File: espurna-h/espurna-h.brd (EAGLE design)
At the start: 50 x 50 mm, 51 parts, among them IC1 AMS1117-3.3, IC2 ESP-12-SMD, IC3 PC817CS, IC4 HLW8012

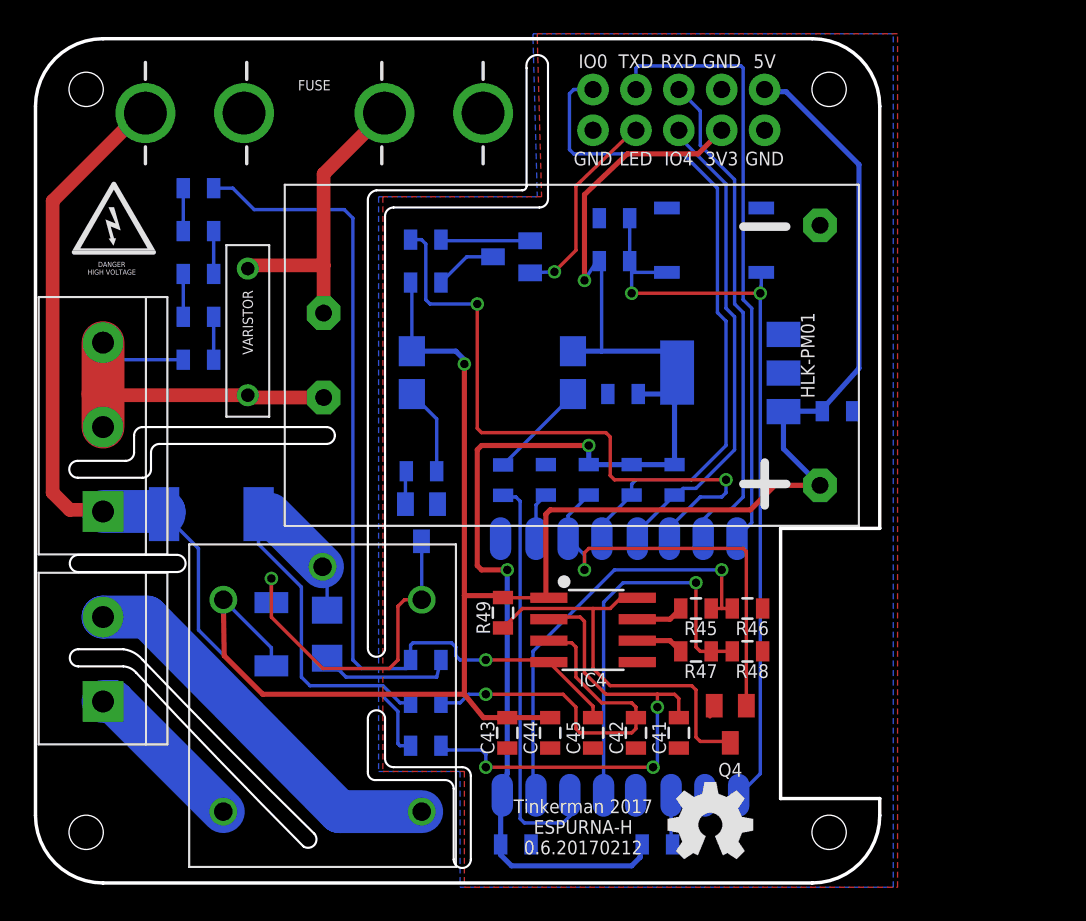
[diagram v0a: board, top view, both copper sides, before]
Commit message: Swapped GPIO2 and GPIO5 to avoid the module LED to change with HLW8012 SEL pin value
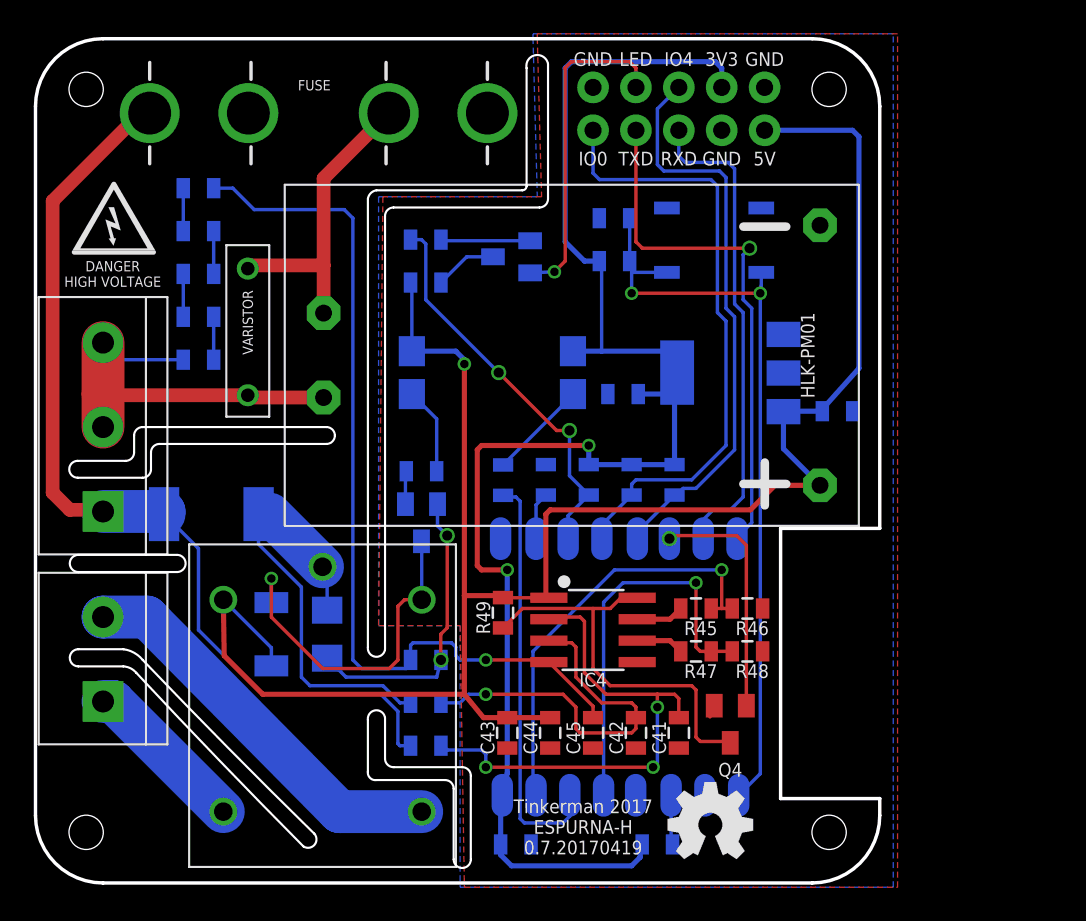
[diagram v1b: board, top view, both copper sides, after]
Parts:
- moved JP22 2.54 mm to (33.0, 47.1)
- moved JP21 2.41 mm to (33.0, 44.6)
- moved FUSE 0.25 mm to (16.8, 45.6)
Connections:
- net GPIO2: now also R27.2; no longer Q4.1
- net GPIO5: now also Q4.1; no longer R27.2
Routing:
- net GPIO5: track 37.8 -> 14.4 mm, vias 2 -> 1
- net GND: track 8.81 -> 18.4 mm, vias 0 -> 2
- net LED: track 11.9 -> 19.4 mm
- net 3V3: track 86.9 -> 94.0 mm, vias 3 -> 2
- net GPIO4: track 28.5 -> 34.0 mm
- net TXD: track 36.2 -> 31.4 mm, vias 0 -> 1
- net GPIO0: track 40.5 -> 36.3 mm
- net GPIO2: track 25.3 -> 23.4 mm, vias 1 -> 2
- net RXD: track 29.8 -> 28.8 mm
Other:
- board text added: "Tinkerman 2017 ESPURNA-H 0.7.20170419"
- board text removed: "Tinkerman 2017 ESPURNA-H 0.6.20170212"

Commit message: Change varistor symbol, added thermal fuse, change measurement point
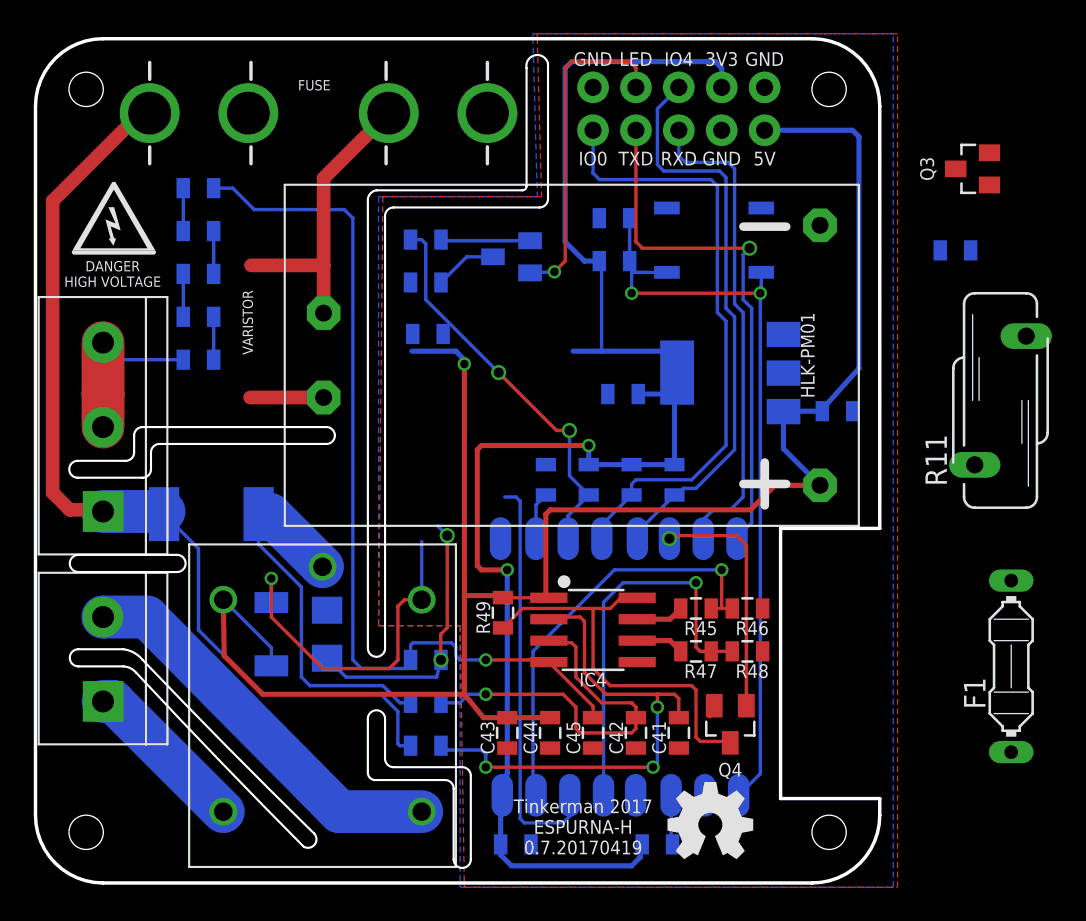
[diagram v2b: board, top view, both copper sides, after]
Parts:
- removed IC3: PC817CS, optocoupler:SMD4-7
- removed VARISTOR: V18ZA2P, SparkFun-DiscreteSemi:V18ZA2P
- added F1: 73C, fuse:PICOFUSE
- added R11: S10K250, varistor:S10K250
- Q3: device xose:SOT23 -> xose:SOT23-WIDE
- R31: value 220 -> 1K
- R32: value 1K -> 10K
- moved Q3 38.8 mm to (55.5, 42.3), flipped to the top, turned to 90 degrees
- moved R31 30.0 mm to (54.5, 37.5), turned to 0 degrees
- moved R32 8.14 mm to (23.2, 32.5)
- renumbered FUSE to F2
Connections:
- removed net N$15: IC3.2, R31.1
- removed net N$6: IC3.3, R32.1
- removed net N$8: F2.3, U$1.AC_L, VARISTOR.P$2
- new net LINE3: R1.1, R42.2, R44.2, RLY1.COMMON
- new net N$7: F1.2, F2.1
- net 3V3: no longer IC3.1
- net 5V: no longer IC3.4
- net GND: now also R32.1
- net GPIO12: now also R31.1; no longer R31.2
- net LINE1: now also F1.1; no longer F2.1, R1.2, R43.2
- net LINE2: now also F2.3, R1.2, R11.2, R43.2, U$1.AC_L; no longer R1.1, R42.2, R44.2, RLY1.COMMON
- net N$5: now also R31.2
- net NEUTRAL: now also R11.1; no longer VARISTOR.P$1
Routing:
- net LINE1: track 56.6 -> 31.7 mm
- net LINE3: track 0.00 -> 22.6 mm
- net N$8: track 18.0 -> 0.00 mm
- net LINE2: track 25.6 -> 42.0 mm
- net NEUTRAL: track 23.3 -> 14.6 mm
- net N$15: track 5.91 -> 0.00 mm
- net N$6: track 5.18 -> 0.00 mm
- net 5V: track 114.0 -> 110.0 mm
- net N$5: track 1.97 -> 0.00 mm
- net GND: track 18.4 -> 17.1 mm

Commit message: Separate power from load. Wire
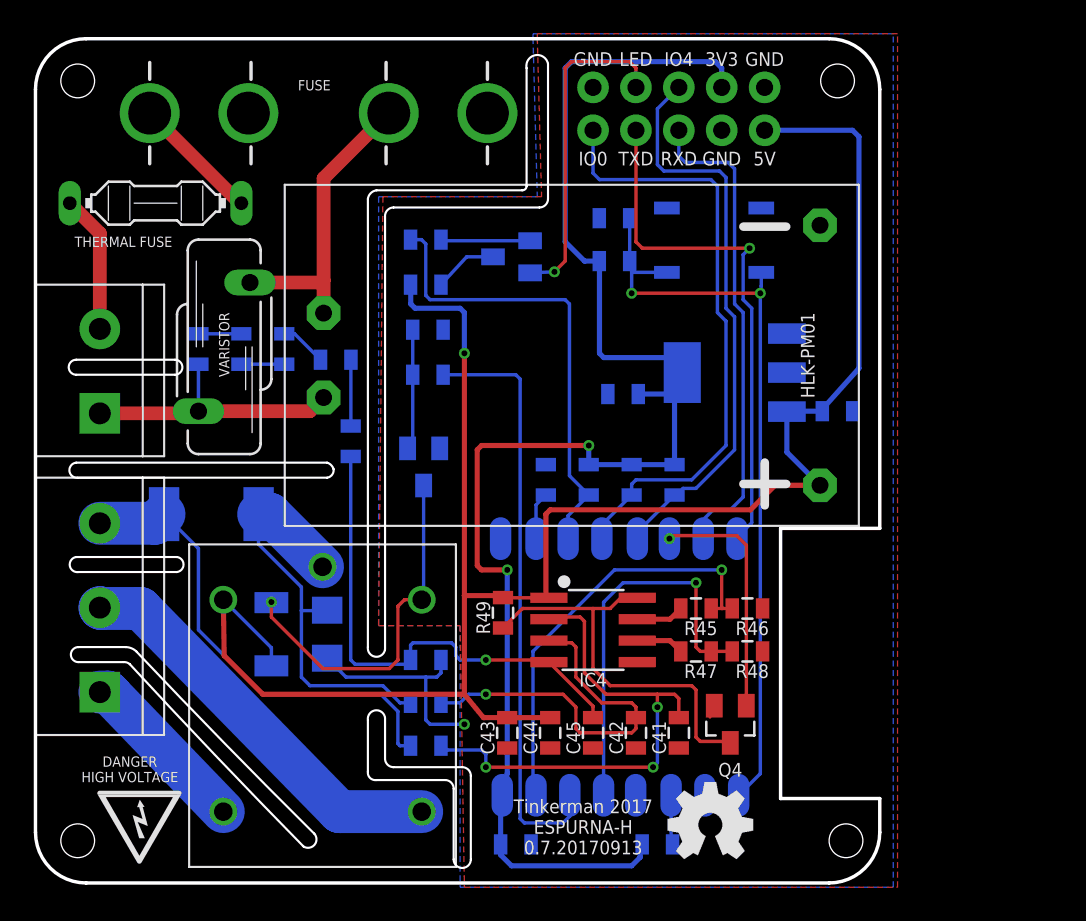
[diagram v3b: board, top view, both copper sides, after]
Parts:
- removed JP1: (no value), xose:SCREWTERMINAL-200MIL-3
- removed JP3: (no value), xose:SCREWTERMINAL-200MIL-2
- added JP2: (no value), xose:SCREWTERMINAL-200MIL-2
- added JP4: (no value), xose:SCREWTERMINAL-200MIL-3
- added U$2, U$3, U$4, U$5: (no value), xose:HOLE_M2_WIDE
- Q3: device xose:SOT23-WIDE -> xose:SOT23
- R11: device varistor:S10K250 -> xose:S10K250
- moved F1 57.6 mm to (7.11, 40.3), turned to 0 degrees
- moved R11 46.1 mm to (11.2, 31.8)
- moved Q3 37.0 mm to (23.0, 24.6), flipped to the bottom, turned to 180 degrees
- moved R31 32.1 mm to (23.2, 30.1)
- moved R55 17.5 mm to (18.7, 26.2), turned to 270 degrees
- moved R54 11.1 mm to (17.8, 31.0), turned to 0 degrees
- moved R53 6.75 mm to (14.7, 31.6), turned to 90 degrees
- moved R52 3.17 mm to (12.2, 31.6), turned to 90 degrees
- moved R51 0.64 mm to (9.65, 31.6), turned to 90 degrees
- moved IC1 0.25 mm to (41.4, 30.2)
- moved R32 0.25 mm to (23.2, 32.8)
- moved R28 0.13 mm to (23.1, 35.4)
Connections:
- net LINE3 renamed LINE_L
- removed net LINE1: F1.1, JP1.1
- removed net LINE2: F2.3, R1.2, R11.2, R43.2, U$1.AC_L
- new net LINE_I: F1.1, JP2.2
- new net LINE_M: JP4.3, R1.2, R43.2
- new net LINE_P: F2.3, R11.2, U$1.AC_L
- net NC: now also JP4.2; no longer JP3.2
- net NEUTRAL: now also JP2.1; no longer JP1.2, JP1.3
- net NO: now also JP4.1; no longer JP3.1
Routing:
- net LINE2: track 42.0 -> 0.00 mm
- net LINE1: track 31.7 -> 0.00 mm
- net LINE_M: track 0.00 -> 28.2 mm
- net V2P: track 53.5 -> 30.2 mm
- net LINE_P: track 0.00 -> 17.9 mm
- net GPIO12: track 24.3 -> 35.1 mm
- net LINE_I: track 0.00 -> 8.18 mm
- net N$7: track 0.00 -> 7.64 mm
- net N$5: track 0.00 -> 7.15 mm
- net 5V: track 110.0 -> 114.3 mm
- net GPIO2: track 23.4 -> 27.7 mm, vias 2 -> 0
- net GND: track 17.1 -> 13.8 mm, vias 2 -> 1
- net LINE_L: track 22.6 -> 24.8 mm
- net 3V3: track 94.0 -> 92.1 mm
- net NEUTRAL: track 14.6 -> 16.4 mm
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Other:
- outline, holes or cut-outs redrawn
- board text added: "THERMAL FUSE"
- board text added: "Tinkerman 2017 ESPURNA-H 0.7.20170913"
- board text removed: "Tinkerman 2017 ESPURNA-H 0.7.20170419"

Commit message: Version 0.7.20170913
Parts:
- removed R1: 0.001R, xose:2512
- added R41: 0.001R, xose:2512
- added V11: S10K250, xose:S10K250
- R11: value S10K250 -> 0R; device xose:S10K250 -> xose:1206
- R42: value 0 -> 0R
- moved R54 10.7 mm to (22.9, 21.6)
- moved R55 8.25 mm to (22.9, 19.1), turned to 0 degrees
- moved R53 7.50 mm to (17.8, 24.8), turned to 0 degrees
- moved R52 7.27 mm to (14.6, 24.8), turned to 0 degrees
- moved R51 7.08 mm to (11.4, 24.8), turned to 0 degrees
- moved R11 3.21 mm to (8.13, 32.8), flipped to the bottom
- moved Q3 2.04 mm to (22.9, 26.7)
- moved D3 0.54 mm to (13.6, 15.1), turned to 90 degrees
- moved F2 0.28 mm to (16.5, 45.7)
- moved R47 0.13 mm to (39.1, 13.8)
- moved R48 0.13 mm to (42.2, 13.8)
- moved F1 0.13 mm to (6.99, 40.3)
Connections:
- removed net N$18: R52.1, R53.1
- removed net N$19: R51.2, R52.2
- new net N$15: R51.1, R52.2
- new net N$16: R52.1, R53.2
- net LINE_I: now also R11.2
- net LINE_L: now also R41.1; no longer R1.1
- net LINE_M: now also R41.2, R51.2; no longer R1.2
- net LINE_P: now also R11.1, V11.2; no longer R11.2
- net N$17: now also R53.1; no longer R53.2
- net NEUTRAL: now also V11.1; no longer R11.1, R51.1
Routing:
- net GND: track 13.8 -> 52.0 mm, vias 1 -> 2
- net V2P: track 30.2 -> 20.5 mm
- net LINE_M: track 28.2 -> 33.8 mm
- net LINE_L: track 24.8 -> 20.1 mm
- net LINE_P: track 17.9 -> 22.1 mm
- net N$17: track 2.78 -> 6.18 mm
- net GPIO5: track 14.4 -> 17.6 mm, vias 1 -> 3
- net LINE_I: track 8.18 -> 11.2 mm
- net NEUTRAL: track 16.4 -> 13.6 mm
- net 5V: track 114.3 -> 111.6 mm
- net N$4: track 21.4 -> 24.0 mm
- net N$19: track 2.54 -> 0.00 mm
- net N$18: track 2.54 -> 0.00 mm
- net N$5: track 7.15 -> 5.17 mm
- net N$6: track 3.93 -> 2.54 mm
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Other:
- outline, holes or cut-outs redrawn
